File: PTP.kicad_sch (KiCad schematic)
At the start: 33 parts, among them CON1 USB MiniB, J1 Conn_01x04_Pin, SW1 SW_SPDT, U1 STM32F103C8T6, U2 USBLC6-2SC6, U3 SPX3819M5-L-3-3, Y1 16MHz

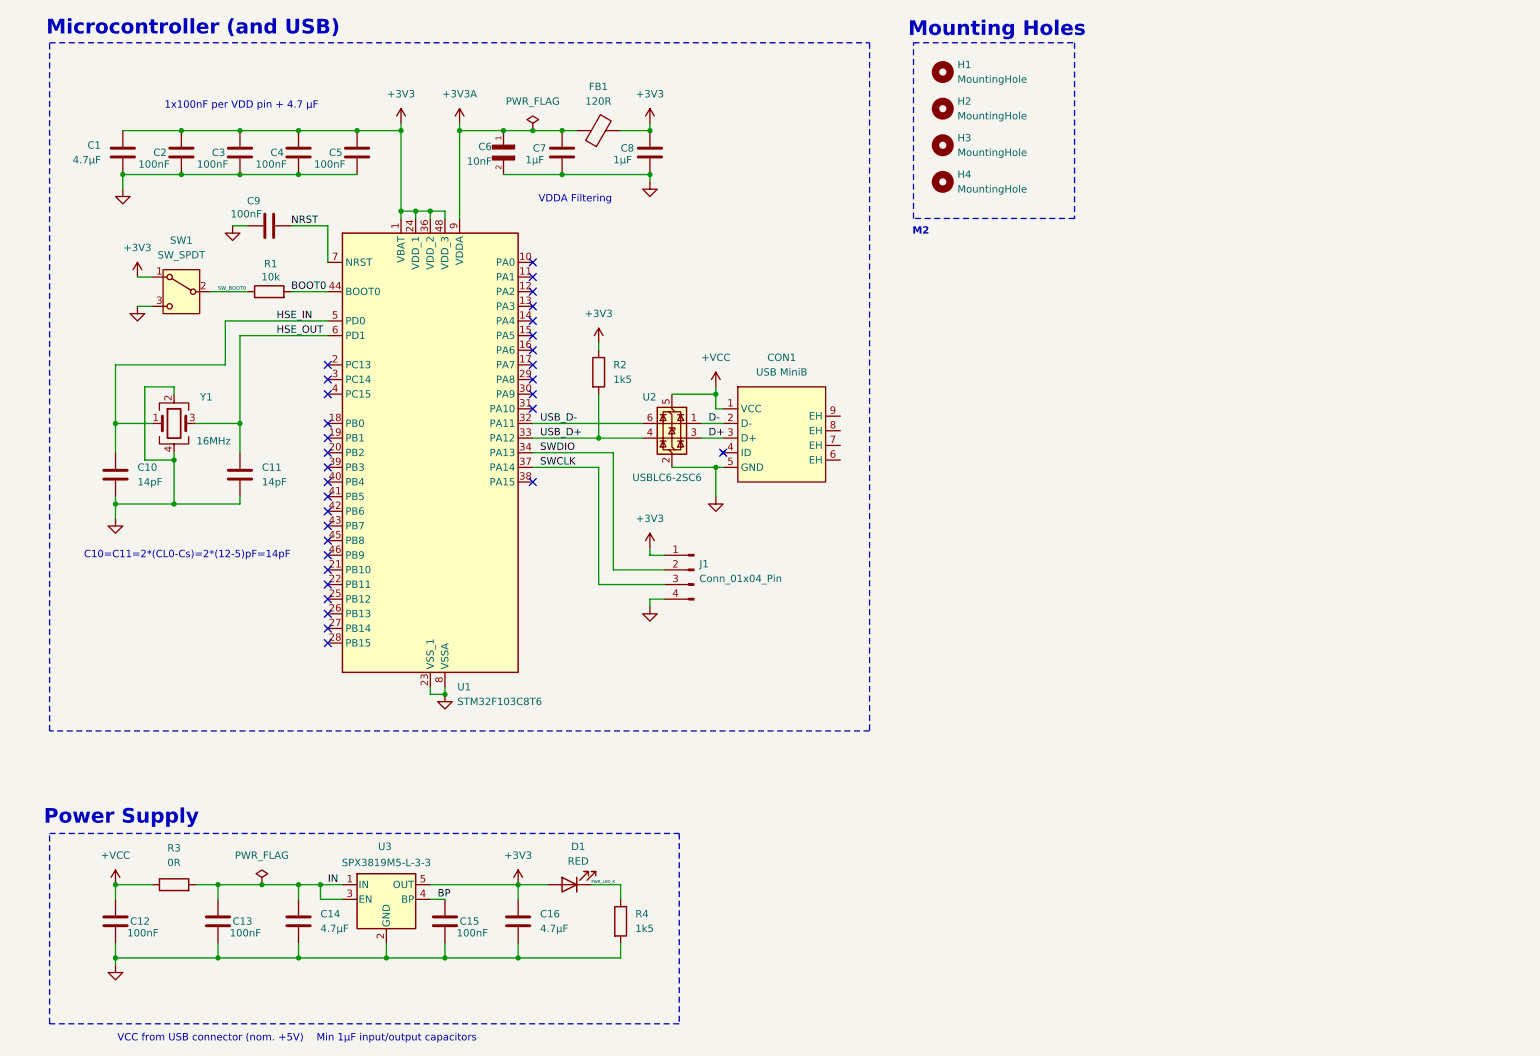
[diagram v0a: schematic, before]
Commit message: v1.1 PTP project - full GPIO breakout, STDC14 port for stlinkv3minie programming
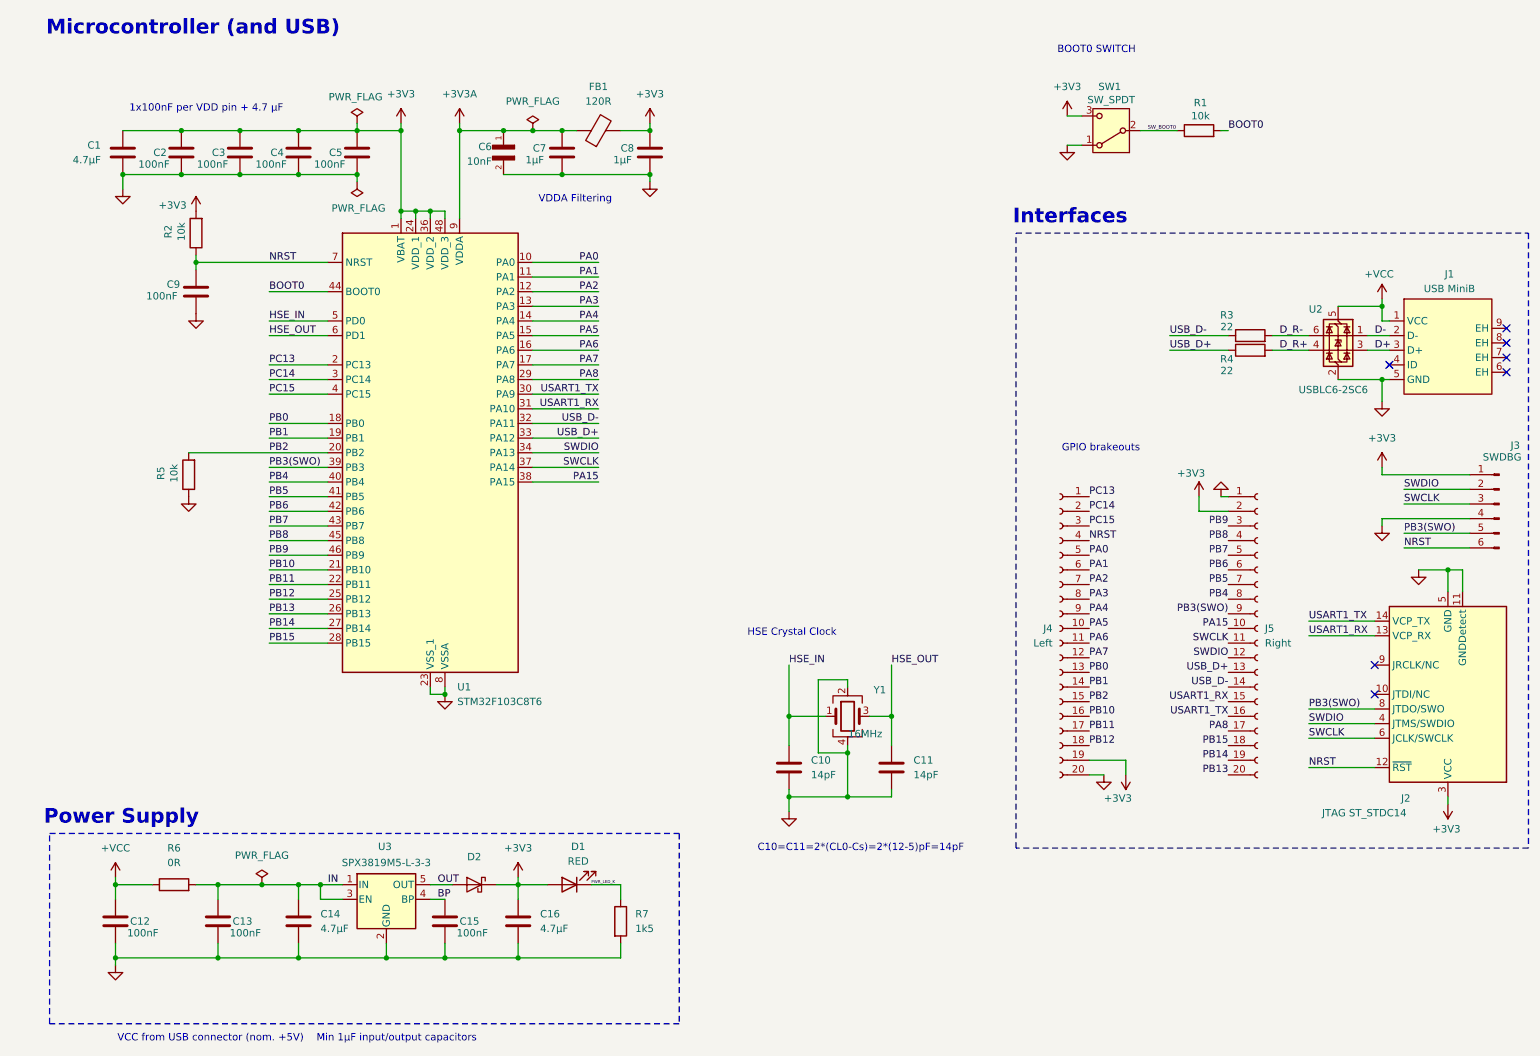
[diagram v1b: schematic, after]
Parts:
- removed H1, H2, H3, H4: MountingHole, MountingHole:MountingHole_2.2mm_M2, symbol Mechanical:MountingHole
- removed J1: Conn_01x04_Pin, Connector_PinSocket_2.54mm:PinSocket_1x04_P2.54mm_Vertical, symbol Connector:Conn_01x04_Pin
- added D2: RB161VA-20TR, Diode_SMD:D_SOD-323, symbol Diode:MBR1020VL
- added J2: JTAG ST_STDC14, PTP_Projekt:FTSH-107-01-L-DV-K, symbol Connector:Conn_ST_STDC14
- added J3: SWDBG, Connector_PinHeader_2.54mm:PinHeader_1x06_P2.54mm_Vertical, symbol Connector:Conn_01x06_Pin
- added J4: Left, Connector_PinHeader_2.54mm:PinHeader_1x20_P2.54mm_Vertical, symbol Connector:Conn_01x20_Socket
- added J5: Right, Connector_PinHeader_2.54mm:PinHeader_1x20_P2.54mm_Vertical, symbol Connector:Conn_01x20_Socket
- added R3, R4: 22, Resistor_SMD:R_0603_1608Metric, symbol Device:R
- added R5: 10k, Resistor_SMD:R_0603_1608Metric, symbol Device:R
- R1: footprint Resistor_SMD:R_1206_3216Metric -> Resistor_SMD:R_0603_1608Metric; JLCPCB P# C1489 -> C188363; Manufacturer UNI-ROYAL(Uniroyal Elec) -> Ever Ohms Tech; P/N 1206W4J0103T5E -> TR0603B10K0P0525Z
- R2: value 1k5 -> 10k; footprint Resistor_SMD:R_0805_2012Metric -> Resistor_SMD:R_0603_1608Metric; JLCPCB P# C4310 -> C188363; Manufacturer UNI-ROYAL(Uniroyal Elec) -> Ever Ohms Tech; P/N 0805W8F1501T5E -> TR0603B10K0P0525Z
- renumbered CON1 to J1, R3 to R6, R4 to R7
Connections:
- net +3V3: now also R2.2, SW1.3 (C), D2.1 (K), J2.3 (VCC), J3.1 (Pin_1), J4.19 (Pin_19), J5.2 (Pin_2); no longer R2.1, SW1.1 (A), U3.5 (OUT)
- net GND: now also SW1.1 (A), J2.11 (GNDDetect), J2.5 (GND), J2.7 (GND), J3.4 (Pin_4), J4.20 (Pin_20), J5.1 (Pin_1), R5.1; no longer SW1.3 (C)
- net NRST: now also R2.1, J2.12 (~{RST}), J3.6 (Pin_6), J4.4 (Pin_4)
- net SWCLK: now also J2.6 (JCLK/SWCLK), J3.3 (Pin_3), J5.11 (Pin_11)
- net SWDIO: now also J2.4 (JTMS/SWDIO), J3.2 (Pin_2), J5.12 (Pin_12)
- net USB_D+: now also J5.13 (Pin_13), R4.1; no longer R2.2, U2.4 (I/O2)
- net USB_D-: now also J5.14 (Pin_14), R3.1; no longer U2.6 (I/O1)
- net PA0: now reaches U1.10 (PA0)
- net PA0: now also J4.5 (Pin_5)
- net PA1: now reaches U1.11 (PA1)
- net PA1: now also J4.6 (Pin_6)
- net PA2: now reaches U1.12 (PA2)
- net PA2: now also J4.7 (Pin_7)
- net PA3: now reaches U1.13 (PA3)
- net PA3: now also J4.8 (Pin_8)
- net PA4: now reaches U1.14 (PA4)
- net PA4: now also J4.9 (Pin_9)
- net PA5: now reaches U1.15 (PA5)
- net PA5: now also J4.10 (Pin_10)
- net PA6: now reaches U1.16 (PA6)
- net PA6: now also J4.11 (Pin_11)
- net PA7: now reaches U1.17 (PA7)
- net PA7: now also J4.12 (Pin_12)
- net PB0: now reaches U1.18 (PB0)
- net PB0: now also J4.13 (Pin_13)
- net PB1: now reaches U1.19 (PB1)
- net PB1: now also J4.14 (Pin_14)
- net PC13: now reaches U1.2 (PC13)
- net PC13: now also J4.1 (Pin_1)
- net PB2: now reaches U1.20 (PB2)
- net PB2: now also J4.15 (Pin_15), R5.2
- net PB10: now reaches U1.21 (PB10)
- net PB10: now also J4.16 (Pin_16)
- net PB11: now reaches U1.22 (PB11)
- net PB11: now also J4.17 (Pin_17)
- net PB12: now reaches U1.25 (PB12)
- net PB12: now also J4.18 (Pin_18)
- net PB13: now reaches U1.26 (PB13)
- net PB13: now also J5.20 (Pin_20)
- net PB14: now reaches U1.27 (PB14)
- net PB14: now also J5.19 (Pin_19)
- net PB15: now reaches U1.28 (PB15)
- net PB15: now also J5.18 (Pin_18)
- net PA8: now reaches U1.29 (PA8)
- net PA8: now also J5.17 (Pin_17)
- net PC14: now reaches U1.3 (PC14)
- net PC14: now also J4.2 (Pin_2)
- net USART1_TX: now reaches U1.30 (PA9)
- net USART1_TX: now also J2.14 (VCP_TX), J5.16 (Pin_16)
- net USART1_RX: now reaches U1.31 (PA10)
- net USART1_RX: now also J2.13 (VCP_RX), J5.15 (Pin_15)
- net PA15: now reaches U1.38 (PA15)
- net PA15: now also J5.10 (Pin_10)
- net PB3(SWO): now reaches U1.39 (PB3)
- net PB3(SWO): now also J2.8 (JTDO/SWO), J3.5 (Pin_5), J5.9 (Pin_9)
- net PC15: now reaches U1.4 (PC15)
- net PC15: now also J4.3 (Pin_3)
- net PB4: now reaches U1.40 (PB4)
- net PB4: now also J5.8 (Pin_8)
- net PB5: now reaches U1.41 (PB5)
- net PB5: now also J5.7 (Pin_7)
- net PB6: now reaches U1.42 (PB6)
- net PB6: now also J5.6 (Pin_6)
- net PB7: now reaches U1.43 (PB7)
- net PB7: now also J5.5 (Pin_5)
- net PB8: now reaches U1.45 (PB8)
- net PB8: now also J5.4 (Pin_4)
- net PB9: now reaches U1.46 (PB9)
- net PB9: now also J5.3 (Pin_3)
- new net D_R+: R4.2, U2.4 (I/O2)
- new net D_R-: R3.2, U2.6 (I/O1)
- new net OUT: D2.2 (A), U3.5 (OUT)
- no-connect marks 32 -> 7
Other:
- note added: "BOOT0 SWITCH"
- note added: "GPIO brakeouts"
- note added: "HSE Crystal Clock"
- note added: "Interfaces"
- note removed: "M2"
- note removed: "Mounting Holes"
- moved on the sheet: C10, C11, C9, J1, R1, SW1, U2, Y1
